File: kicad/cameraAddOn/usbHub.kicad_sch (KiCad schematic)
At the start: 28 parts, among them SW1 B3U-1000P[], U4 USB2513B-AEZC, U6 NCP1529A

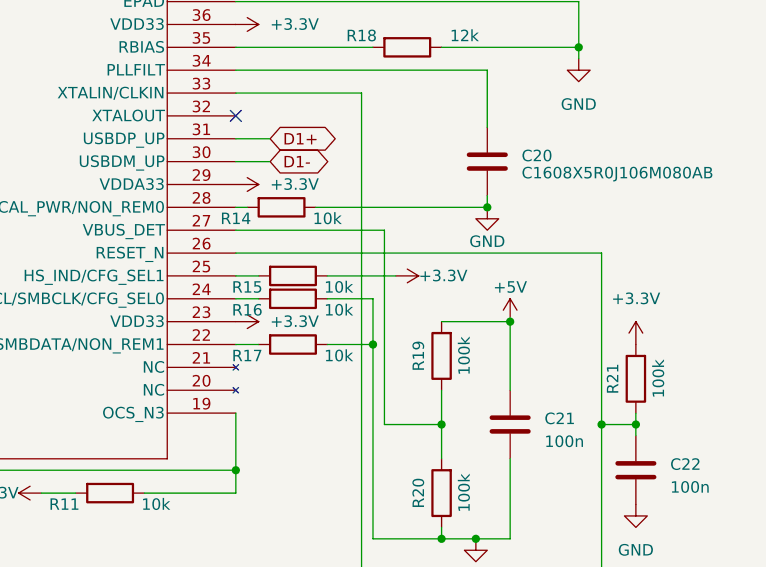
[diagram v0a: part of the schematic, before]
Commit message: V1.1 of perifAddOn (added bus-switch on sd-card)
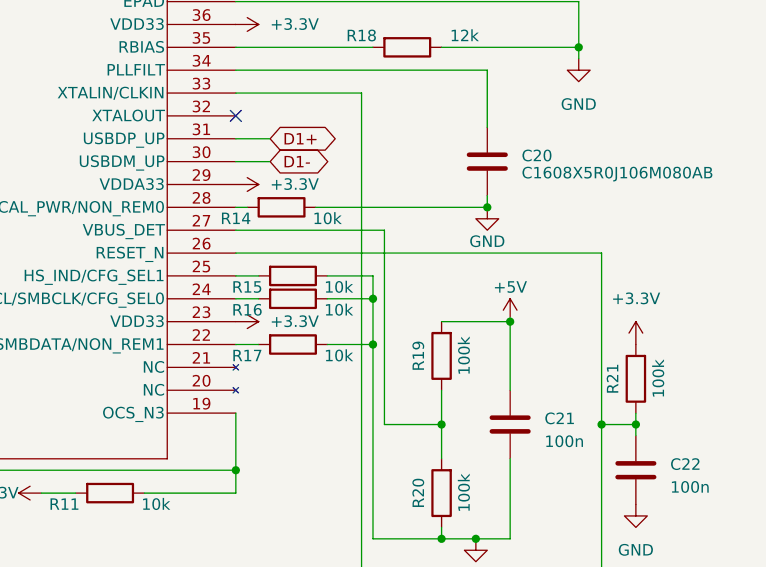
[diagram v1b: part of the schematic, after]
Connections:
- net +3.3V: no longer R15.1
- net GND: now also R15.1
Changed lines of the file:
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@@
   (junction (at 114.3 97.79) (diameter 0) (color 0 0 0 0)
+  )
+  (junction (at 243.84 55.88) (diameter 0) (color 0 0 0 0)
   )
   (junction (at 137.16 120.65) (diameter 0) (color 0 0 0 0)
@@
     (stroke (width 0) (type default))
   )
+  (wire (pts (xy 238.76 53.34) (xy 243.84 53.34))
+    (stroke (width 0) (type default))
+  )
   (wire (pts (xy 256.54 30.48) (xy 256.54 36.83))
     (stroke (width 0) (type default))
@@
     (stroke (width 0) (type default))
   )
+  (wire (pts (xy 243.84 53.34) (xy 243.84 55.88))
+    (stroke (width 0) (type default))
+  )
   (wire (pts (xy 91.44 83.82) (xy 97.79 83.82))
     (stroke (width 0) (type default))
@@
   )
   (wire (pts (xy 97.79 97.79) (xy 102.87 97.79))
-    (stroke (width 0) (type default))
-  )
-  (wire (pts (xy 238.76 53.34) (xy 246.38 53.34))
     (stroke (width 0) (type default))
   )
@@
         )
       )
-    )
-  )
-  (symbol (lib_id "power:+3.3V") (at 246.38 53.34 270) (unit 1)
-    (in_bom yes) (on_board yes) (dnp no)
-    (property "Reference" "#PWR040" (at 242.57 53.34 0)
-      (effects (font (size 1.27 1.27)) hide)
-    )
-    (property "Value" "+3.3V" (at 248.92 53.34 90)
-      (effects (font (size 1.27 1.27)) (justify left))
-    )
-    (property "Footprint" "" (at 246.38 53.34 0)
-      (effects (font (size 1.27 1.27)) hide)
-    )
-    (property "Datasheet" "" (at 246.38 53.34 0)
-      (effects (font (size 1.27 1.27)) hide)
-    )
-    (pin "1")
-    (instances
-      (project "addOnTemplate"
-        (path "/c4a49e8d-4344-49ad-8b55-370a9310fd4c/cc59d6f0-e7f3-42e1-af68-cb40c350ce38"
-          (reference "#PWR040") (unit 1)
-        )
-      )
